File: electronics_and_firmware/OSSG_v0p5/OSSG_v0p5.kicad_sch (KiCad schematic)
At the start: 38 parts, among them J1 Conn_01x05_Male, J2 Ext RGB, J4 Touch, J5 Ext. HUD (experimental), Q1 2SC4617R BR, Q2 2SC4617R BR, SW1 SW_SPST, U1 MP23DB01HPTR, U2 ESP32-PICO-D4, U3 CH9102F, U9 LY68L6400SLIT_PSRAM

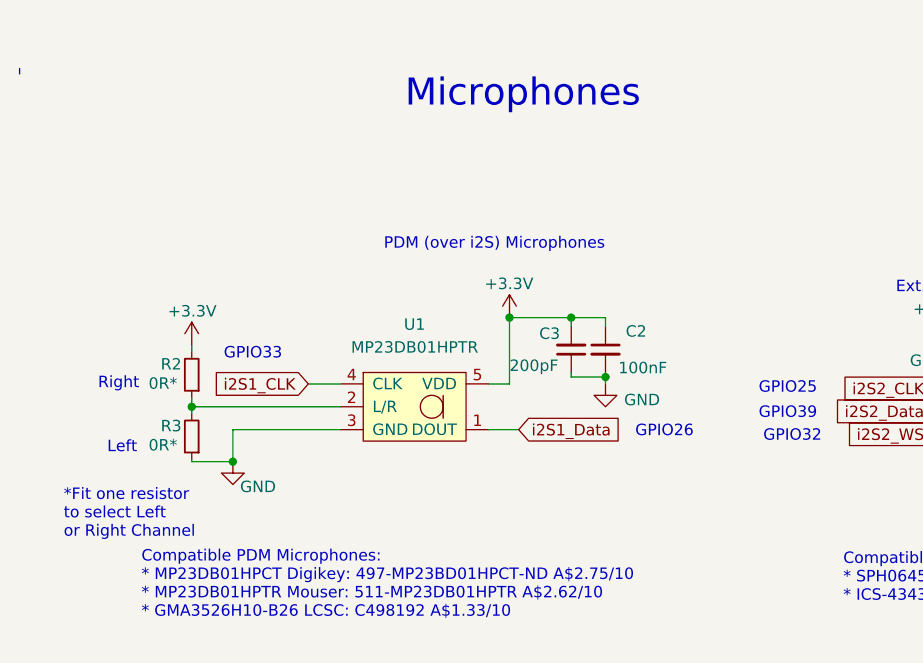
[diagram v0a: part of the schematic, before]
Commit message: move pcb shape notch to top, swap mic for i2s mic
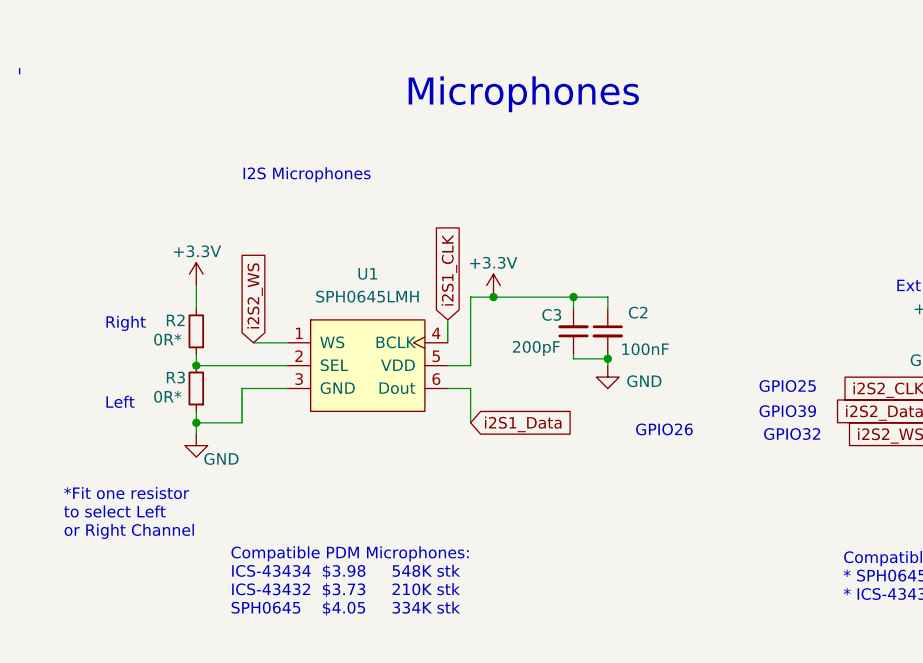
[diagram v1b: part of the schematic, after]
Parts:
- removed U1: MP23DB01HPTR, OSSG_footprints:MP23DB01HPTR, symbol OSSG_components_lib:MP23DB01HPTR
- added U1: SPH0645LMH, OSSG_footprints:SPH0645LM4H-B-SMD-GND, symbol OSSG_components_lib:SPH0645LMH
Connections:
- net +3V3: now also U1.5 (VDD)
- net GND: now also U1.3 (GND)
- net i2S1_CLK: now also U1.4 (BCLK)
- net i2S1_Data: now also U1.6 (Dout)
- net i2S2_WS: now also U1.1 (WS)
- net at R2.1, R3.2: now also U1.2 (SEL)
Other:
- note added: "Compatible PDM Microphones: ICS-43434 $3.98 548K stk ICS-43432 $3.73 210K stk SPH0645 $4.05 334K stk"
- note added: "I2S Microphones"
- note removed: "Compatible PDM Microphones: * MP23DB01HPCT Digikey: 497-MP23BD01HPCT-ND A$2.75/10 * MP23DB01HPTR Mouser: 511-MP23DB01HPTR A$2.62/10 * GMA3526H10-B26 LCSC: C498192 A$1.33/10"
- note removed: "GPIO33"
- note removed: "PDM (over i2S) Microphones"
- moved on the sheet: C2, C3, R2, R3

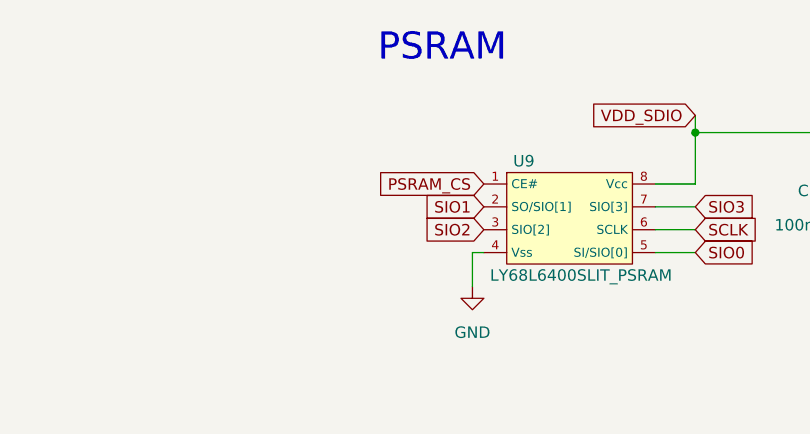
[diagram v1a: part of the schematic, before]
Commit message: fix issues, fix silk screen, add psram pullup, change i2s mic footprint, change battery charging resistor, make notch bigger and fix 3v3 pour not contiguous
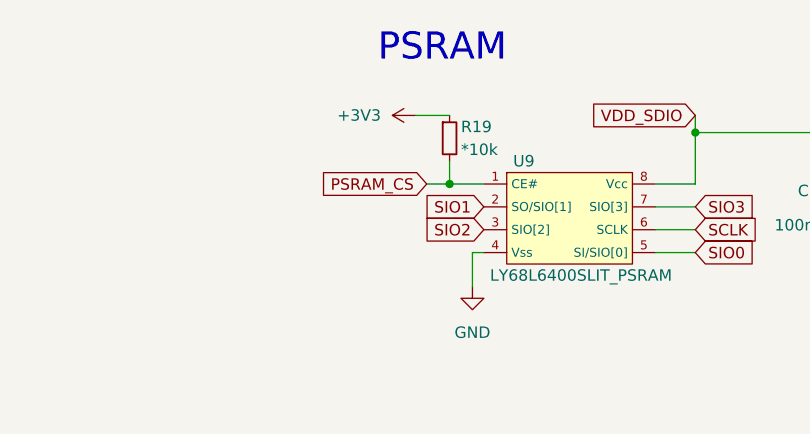
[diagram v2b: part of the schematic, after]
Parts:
- added R19: *10k, Resistor_SMD:R_0402_1005Metric, symbol Device:R_Small
- U1: footprint OSSG_footprints:SPH0645LM4H-B-SMD-GND -> OSSG_footprints:MIC_SPH0645LM4H-B
- U9: LCSCLink (none) -> https://www.lcsc.com/product-detail/RAM_Lyontek-Inc-LY68L64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; MPN_LCSC (none) -> C261881
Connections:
- net +3V3: now also R19.1
- net PSRAM_CS: now also R19.2
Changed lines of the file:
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@@
   (junction (at 207.518 127.254) (diameter 0) (color 0 0 0 0)
+  )
+  (junction (at 168.91 41.91) (diameter 0) (color 0 0 0 0)
   )
   (junction (at 91.44 44.45) (diameter 0) (color 0 0 0 0)
@@
     (stroke (width 0) (type default) (color 0 0 0 0))
   )
+  (wire (pts (xy 165.1 34.29) (xy 168.91 34.29))
+    (stroke (width 0) (type default) (color 0 0 0 0))
+  )
   (wire (pts (xy 148.59 114.554) (xy 147.32 114.554))
     (stroke (width 0) (type default) (color 0 0 0 0))
@@
     (stroke (width 0) (type default) (color 0 0 0 0))
   )
+  (wire (pts (xy 168.91 39.37) (xy 168.91 41.91))
+    (stroke (width 0) (type default) (color 0 0 0 0))
+  )
   (wire (pts (xy 150.7998 197.231) (xy 152.527 197.231))
     (stroke (width 0) (type default) (color 0 0 0 0))
@@
     (stroke (width 0) (type default) (color 0 0 0 0))
   )
+  (wire (pts (xy 166.37 41.91) (xy 168.91 41.91))
+    (stroke (width 0) (type default) (color 0 0 0 0))
+  )
   (wire (pts (xy 165.1 202.311) (xy 162.9156 202.311))
     (stroke (width 0) (type default) (color 0 0 0 0))
@@
   )
   (wire (pts (xy 309.118 110.998) (xy 309.118 111.76))
+    (stroke (width 0) (type default) (color 0 0 0 0))
+  )
+  (wire (pts (xy 168.91 41.91) (xy 172.72 41.91))
     (stroke (width 0) (type default) (color 0 0 0 0))
   )
@@
     )
   )
-  (global_label "PSRAM_CS" (shape input) (at 172.72 41.91 180) (fields_autoplaced)
+  (global_label "PSRAM_CS" (shape input) (at 166.37 41.91 180) (fields_autoplaced)
     (effects (font (size 1.27 1.27)) (justify right))
-    (property "Intersheet References" "${INTERSHEET_REFS}" (id 0) (at 160.5702 41.8306 0)
+    (property "Intersheet References" "${INTERSHEET_REFS}" (id 0) (at 154.2202 41.8306 0)
       (effects (font (size 1.27 1.27)) (justify right) hide)
     )
@@
     (property "Reference" "U1" (id 0) (at 50.8 243.84 0))
     (property "Value" "SPH0645LMH" (id 1) (at 50.8 246.38 0))
-    (property "Footprint" "OSSG_footprints:SPH0645LM4H-B-SMD-GND" (id 2) (at 53.34 245.11 0)
+    (property "Footprint" "OSSG_footprints:MIC_SPH0645LM4H-B" (id 2) (at 53.34 245.11 0)
       (effects (font (size 1.27 1.27)) hide)
     )
@@
     )
     (property "Datasheet" "~" (id 3) (at 166.9034 175.514 0)
+      (effects (font (size 1.27 1.27)) hide)
+    )
+    (pin "1")
+  )
+  (symbol (lib_id "power:+3V3") (at 165.1 34.29 90) (unit 1)
+    (in_bom yes) (on_board yes) (fields_autoplaced)
+    (property "Reference" "#PWR0109" (id 0) (at 168.91 34.29 0)
+      (effects (font (size 1.27 1.27)) hide)
+    )
+    (property "Value" "+3V3" (id 1) (at 161.29 34.2899 90)
+      (effects (font (size 1.27 1.27)) (justify left))
+    )
+    (property "Footprint" "" (id 2) (at 165.1 34.29 0)
+      (effects (font (size 1.27 1.27)) hide)
+    )
+    (property "Datasheet" "" (id 3) (at 165.1 34.29 0)
       (effects (font (size 1.27 1.27)) hide)
     )
@@
     (pin "2")
     (pin "3")
+  )
+  (symbol (lib_id "Device:R_Small") (at 168.91 36.83 0) (unit 1)
+    (in_bom yes) (on_board yes)
+    (property "Reference" "R19" (id 0) (at 170.18 35.56 0)
+      (effects (font (size 1.27 1.27)) (justify left))
+    )
+    (property "Value" "*10k" (id 1) (at 170.18 38.1 0)
+      (effects (font (size 1.27 1.27)) (justify left))
+    )
+    (property "Footprint" "Resistor_SMD:R_0402_1005Metric" (id 2) (at 168.91 36.83 0)
+      (effects (font (size 1.27 1.27)) hide)
+    )
+    (property "Datasheet" "~" (id 3) (at 168.91 36.83 0)
+      (effects (font (size 1.27 1.27)) hide)
+    )
+    (pin "1")
+    (pin "2")
   )
   (symbol (lib_id "power:+3.3V") (at 114.046 251.46 0) (mirror y) (unit 1)
@@
       (effects (font (size 1.27 1.27)) hide)
     )
+    (property "MPN_LCSC" "C261881" (id 4) (at 181.61 45.72 0)
+      (effects (font (size 1.27 1.27)) hide)
+    )
+    (property "LCSCLink" "https://www.lcsc.com/product-detail/RAM_Lyontek-Inc-LY68L6400SLIT_C261881.html" (id 5) (at 181.61 45.72 0)
+      (effects (font (size 1.27 1.27)) hide)
+    )
     (pin "1")
     (pin "2")
@@
       (reference "#PWR0108") (unit 1) (value "GND") (footprint "")
     )
+    (path "/0c5cacc2-83c5-49d1-81f6-c6666fa374e9"
+      (reference "#PWR0109") (unit 1) (value "+3V3") (footprint "")
+    )
     (path "/777464b5-c722-47bf-99d3-1a7994e72d25"
       (reference "AE1") (unit 1) (value "ANT3216LL00R2400A") (footprint "OSSG_footprints:ANT3216LL00R2400A")
@@
     )
     (path "/34a40e42-7107-4de0-9230-08b651254313/e1395c59-2f60-4b2d-bee6-e2e22b1f4ca7"
-      (reference "R8") (unit 1) (value "2K") (footprint "Resistor_SMD:R_0402_1005Metric")
+      (reference "R8") (unit 1) (value "2.2K") (footprint "Resistor_SMD:R_0402_1005Metric")
     )
     (path "/34a40e42-7107-4de0-9230-08b651254313/ceade57a-c25e-4ab8-bf41-a92e98139556"
@@
       (reference "R18") (unit 1) (value "10K") (footprint "Resistor_SMD:R_0402_1005Metric")
     )
+    (path "/af26d7ed-eab2-402d-8b14-5fb5f8827ea1"
+      (reference "R19") (unit 1) (value "*10k") (footprint "Resistor_SMD:R_0402_1005Metric")
+    )
     (path "/92534179-acae-4912-baf5-95c7fd0a3d18"
       (reference "SW1") (unit 1) (value "SW_SPST") (footprint "OSSG_footprints:SMD_Switch_Panasonic_EVQPUL_EVQPUC_6.3x6.7")
@@
     )
     (path "/09f62ead-502a-48ea-9ff1-77fe9ff825f7"
-      (reference "U1") (unit 1) (value "SPH0645LMH") (footprint "OSSG_footprints:SPH0645LM4H-B-SMD-GND")
+      (reference "U1") (unit 1) (value "SPH0645LMH") (footprint "OSSG_footprints:MIC_SPH0645LM4H-B")
     )
     (path "/b136d079-1922-4e2c-b5d7-49459d0477e3"

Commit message: fill in missing LCSC part numbers (still missing polyfuse
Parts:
- D1: LCSCLink (none) -> https://lcsc.com/product-detail/Light-Emitting-Diodes-LED_W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; MPN_LCSC (none) -> C965555
- R19: MPN_LCSC (none) -> C2906885
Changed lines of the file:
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@@
       (effects (font (size 1.27 1.27)) (justify left top) hide)
+    )
+    (property "LCSCLink" "https://lcsc.com/product-detail/Light-Emitting-Diodes-LED_Worldsemi-WS2812B-2020_C965555.html" (id 4) (at 317.5 119.38 0)
+      (effects (font (size 1.27 1.27)) hide)
+    )
+    (property "MPN_LCSC" "C965555" (id 5) (at 317.5 119.38 0)
+      (effects (font (size 1.27 1.27)) hide)
     )
     (pin "1")
@@
     )
     (property "Datasheet" "~" (id 3) (at 168.91 36.83 0)
+      (effects (font (size 1.27 1.27)) hide)
+    )
+    (property "MPN_LCSC" "C2906885" (id 4) (at 168.91 36.83 0)
       (effects (font (size 1.27 1.27)) hide)
     )
@@
     )
     (path "/34a40e42-7107-4de0-9230-08b651254313/e1395c59-2f60-4b2d-bee6-e2e22b1f4ca7"
-      (reference "R8") (unit 1) (value "2.2K") (footprint "Resistor_SMD:R_0402_1005Metric")
+      (reference "R8") (unit 1) (value "2.1k") (footprint "Resistor_SMD:R_0402_1005Metric")
     )
     (path "/34a40e42-7107-4de0-9230-08b651254313/ceade57a-c25e-4ab8-bf41-a92e98139556"

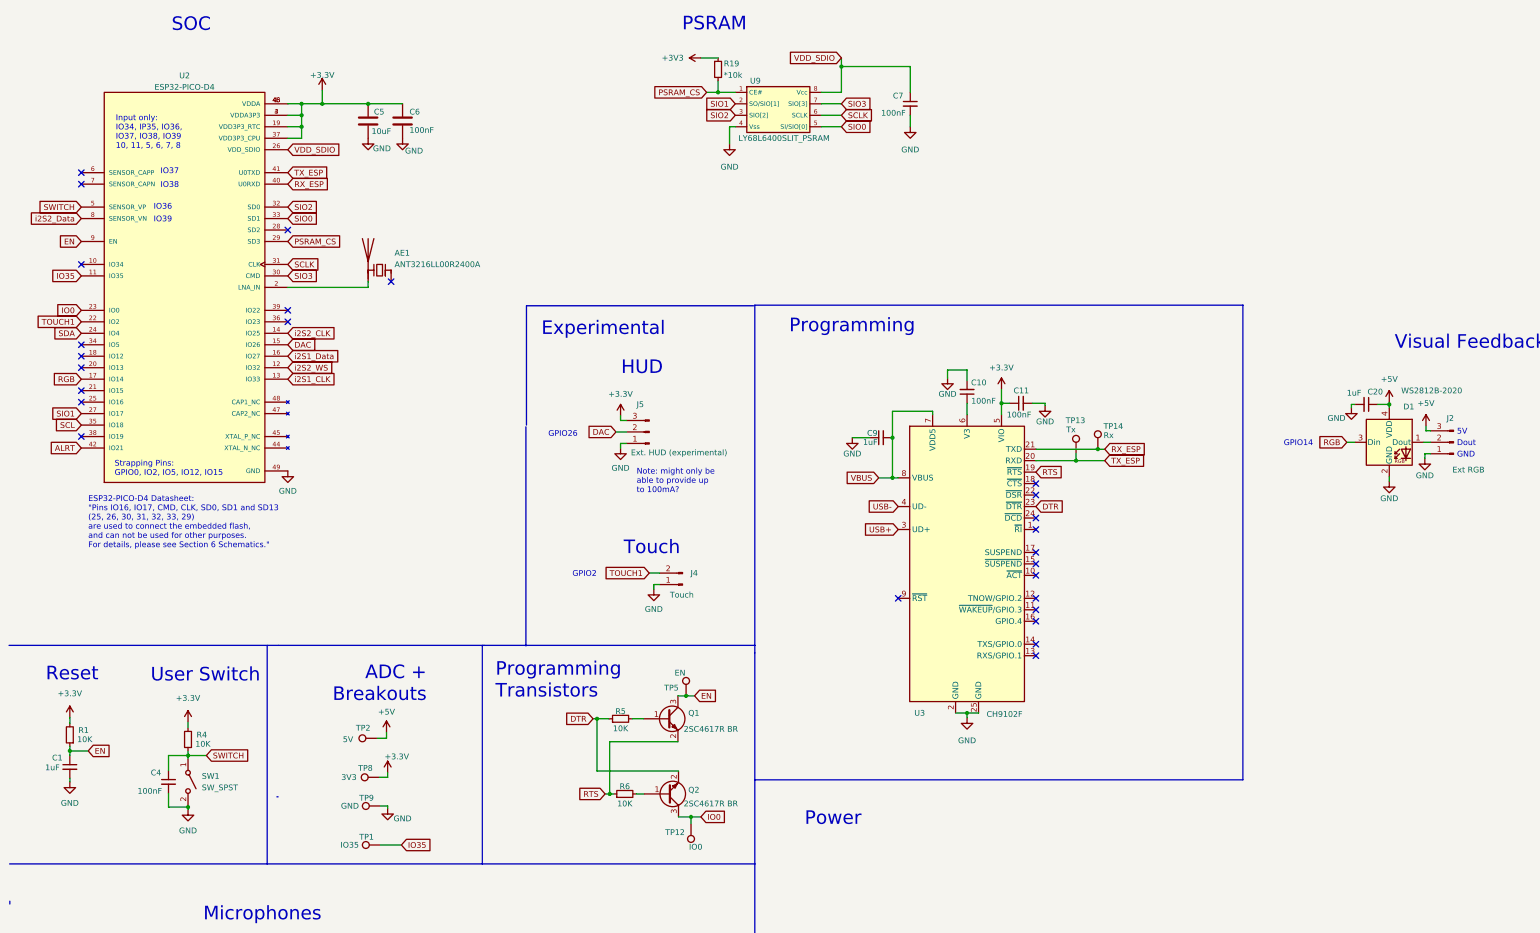
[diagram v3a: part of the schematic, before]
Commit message: add mosfet switch for display power, thicken some traces, check things over
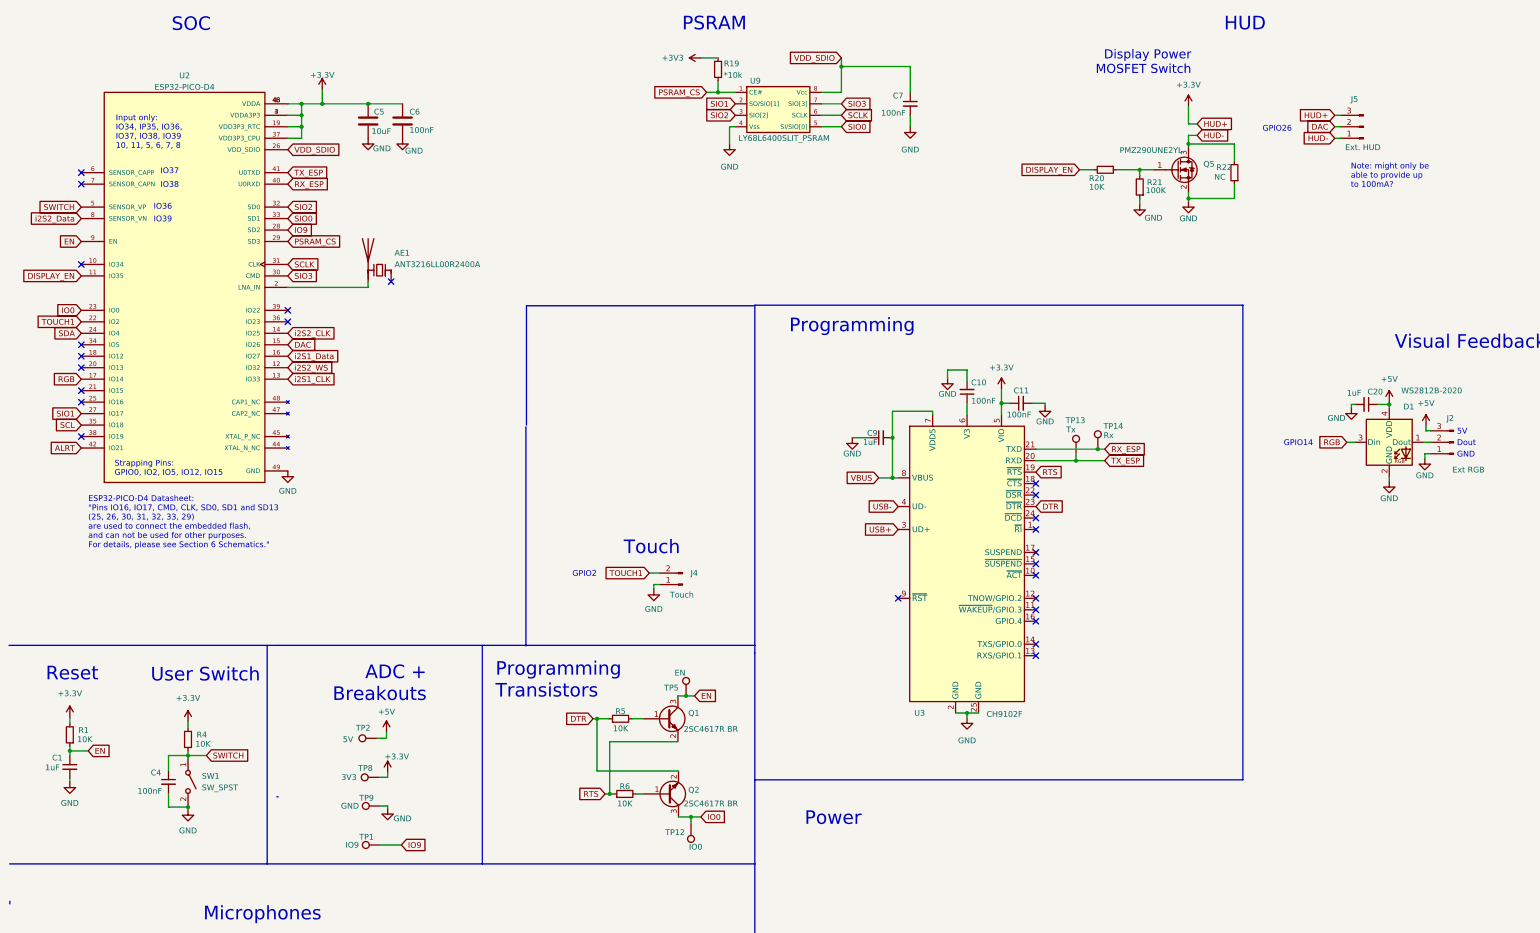
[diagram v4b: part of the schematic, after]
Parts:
- added Q5: PMZ290UNE2YL, OSSG_footprints:DFN100X60X40-3N, symbol OSSG_components_lib:PMZ290UNE2YL
- added R20: 10K, Resistor_SMD:R_0402_1005Metric, symbol Device:R_Small
- added R21: 100K, Resistor_SMD:R_0402_1005Metric, symbol Device:R_Small
- added R22: NC, Resistor_SMD:R_0402_1005Metric, symbol Device:R_Small
- J5: value Ext. HUD (experimental) -> Ext. HUD
- TP1: value IO35 -> IO9
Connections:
- net GND: now also Q5.2 (S), R21.1, R22.1; no longer J5.1 (Pin_1)
- net IO9: now reaches U2.28 (SD2)
- net IO9: now also TP1.1
- net IO35 renamed DISPLAY_EN
- net DISPLAY_EN: now also R20.2; no longer TP1.1
- new net: Q5.1 (G), R20.1, R21.2
- new net HUD-: J5.1 (Pin_1), Q5.3 (D), R22.2
- no-connect marks 26 -> 25
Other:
- note added: "Display Power MOSFET Switch"
- note removed: "Experimental"
- moved on the sheet: J5

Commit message: change display MOSFET switch to p-type and switch high, thicken some traces on ext. i2s board, slide button down (check this fits capabilities), get rid of via in pad, move i2s line so not over top of psram lines
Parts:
- removed Q5: PMZ290UNE2YL, OSSG_footprints:DFN100X60X40-3N, symbol OSSG_components_lib:PMZ290UNE2YL
- added Q5: PMZ350UPEYL, OSSG_footprints:DFN100X60X40-3N, symbol OSSG_components_lib:PMZ350UPEYL
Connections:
- net +3V3: now also R22.2, Q5.2 (S); no longer J5.3 (Pin_3)
- net GND: now also J5.1 (Pin_1); no longer R22.1
- net at R20.1, R21.2: now also Q5.1 (G)
- removed net HUD-: J5.1 (Pin_1), R22.2
- new net HUD+: J5.3 (Pin_3), Q5.3 (D), R22.1
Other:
- note added: "Ext. i2S Microphone"
- note added: "Internal I2S Microphone"
- note added: "This is load, which is grounded, see below,"
- note removed: "Compatible PDM Microphones: ICS-43434 $3.98 548K stk ICS-43432 $3.73 210K stk SPH0645 $4.05 334K stk"
- note removed: "Ext. i2S Microphones"
- note removed: "I2S Microphones"
- moved on the sheet: C2, C20, C3, C7, D1, J1, J2, J4, J5, R19, R2, R20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

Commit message: final v0.5 PCB and components order files
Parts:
- Q5: MPN_LCSC (none) -> C478207; Price_LCSC (none) -> 0.0804
- R2: DigiKeyLink https://www.digikey.ca/en/products/detail/stackpole-electro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 -> (none); LCSCLink https://lcsc.com/product-detail/Chip-span-style-background-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 -> (none); MPN RMCF0402JT10K0CT-ND -> (none); MPN_LCSC C2906885 -> C2906877; Price 0.018 -> 0.004; Price_LCSC 0.0005 -> 0.0004
- R22: MPN RMCF0402JT10K0CT-ND -> (none); MPN_LCSC C2906885 -> C2906877; Price 0.018 -> 0.0004; Price_LCSC 0.0005 -> 0.0004
- R3: LCSCLink https://lcsc.com/product-detail/Chip-span-style-background-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 -> (none); MPN RMCF0402JT10K0CT-ND -> (none); MPN_LCSC C2906885 -> C2906877; Price 0.018 -> 0.0004; Price_LCSC 0.0005 -> 0.0004
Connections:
- net +3V3: now also R21.2
- net GND: no longer R21.1
- net at Q5.1 (G), R20.1: now also R21.1; no longer R21.2
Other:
- note added: "0R here to bypass MOSFET switch."
- moved on the sheet: R21
